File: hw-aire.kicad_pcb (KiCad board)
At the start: 2 copper layers, 75 x 60 mm, 58 parts, among them J1 Conn_01x02_Pin, J2 Conn_01x02_Pin, J3 Screw_Terminal_01x12, J4 Conn_01x04_Pin, J5 Conn_01x05_Pin, K1 JRC-21F(4100), K2 JRC-21F(4100), K3 JRC-21F(4100), Q1 PMBT3904235, Q2 PMBT3904235, Q3 PMBT3904235, Q5 PMBT3904235, SW1 SW_Push, U1 HLK-2M05, U2 NCP1117-3.3_SOT223, U3 ESP-12E, U4 SHT4x, U5 BMP581

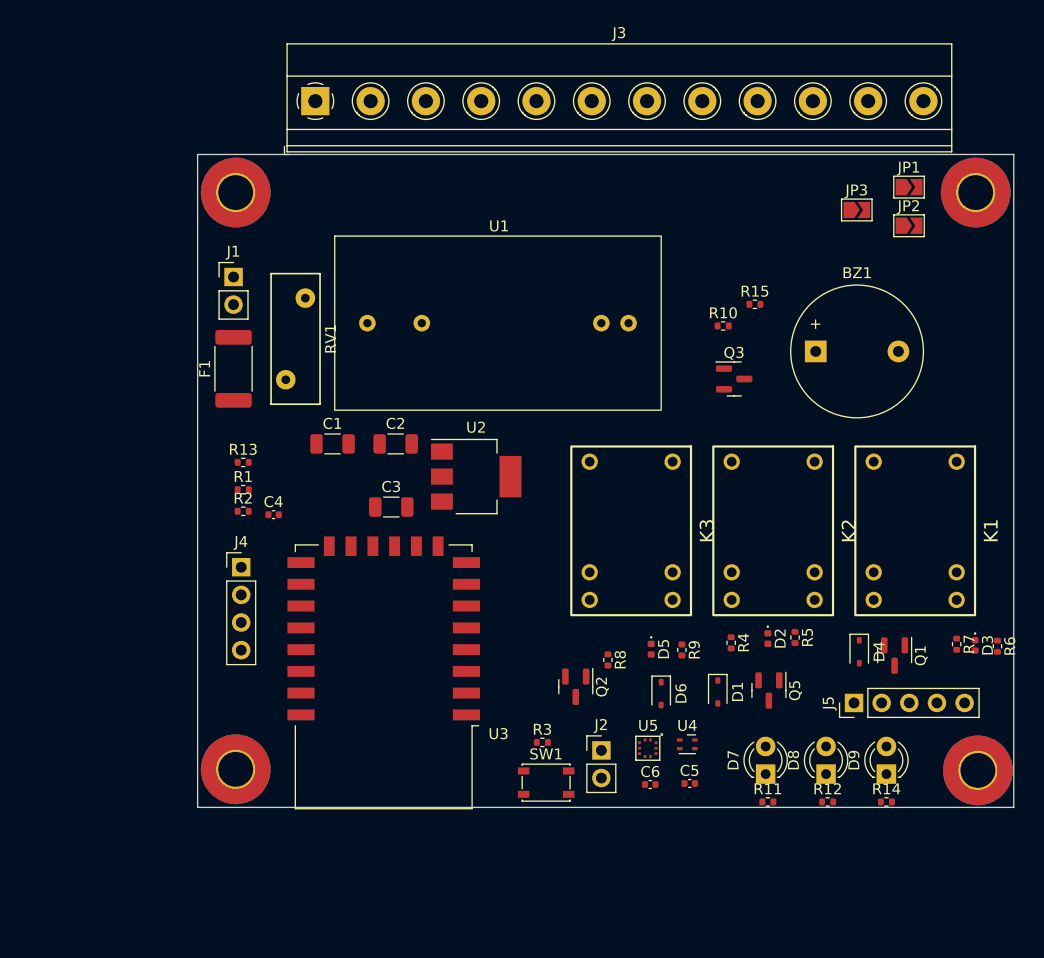
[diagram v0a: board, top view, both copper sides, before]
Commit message: Finish routing and serigraphy. Ready to review
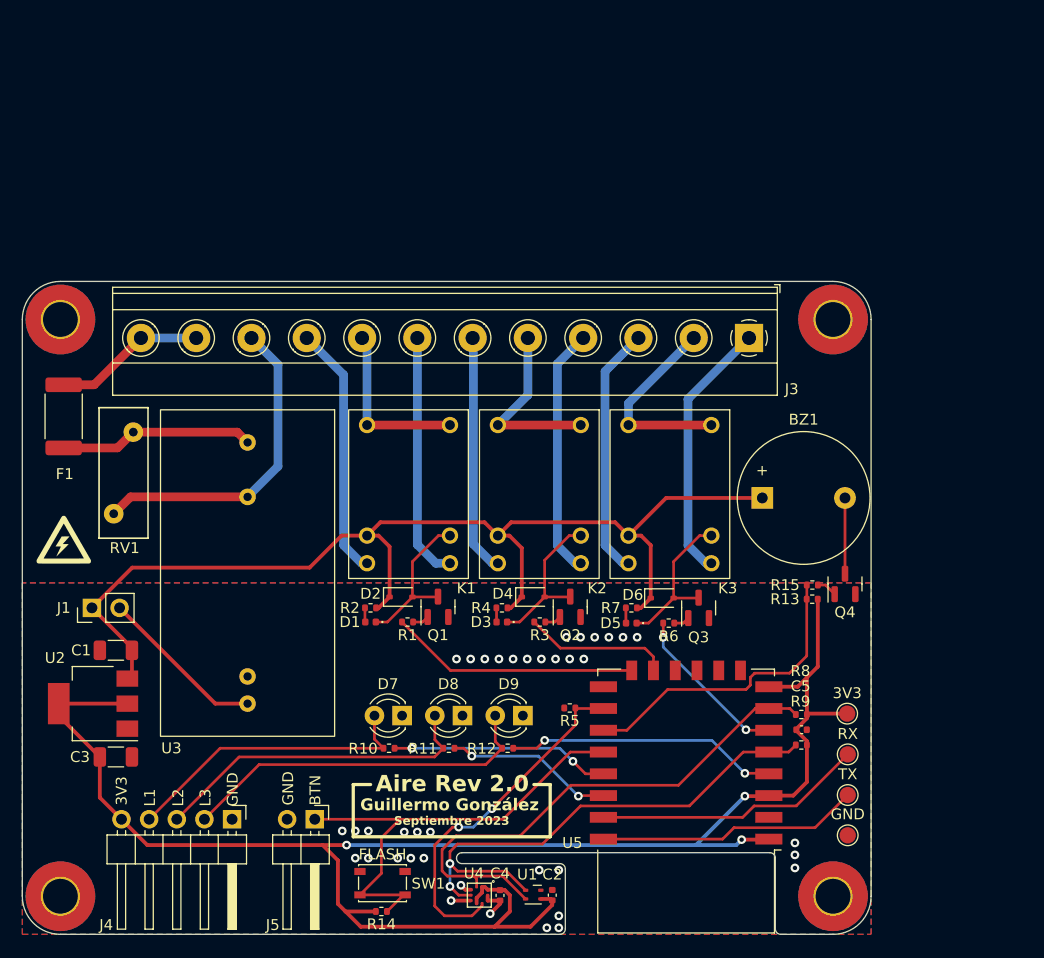
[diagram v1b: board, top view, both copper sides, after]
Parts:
- removed the C3 at (140.7, 87.6)
- removed the J4 at (126.9, 93.1)
- removed JP1, JP2, JP3: SolderJumper_2_Open, Jumper:SolderJumper-2_P1.3mm_Open_TrianglePad1.0x1.5mm
- added G***: LOGO, guille-lib:high_voltage_5mm, F.Cu at (110.6, 90.6)
- added G***: LOGO, guille-lib:high_voltage, B.Cu at (121.6, 88.2)
- added TP1: TestPoint, TestPoint:TestPoint_Pad_D1.5mm, F.Cu at (182.6, 114.1)
- added TP2: TestPoint, TestPoint:TestPoint_Pad_D1.5mm, F.Cu at (182.6, 110.3)
- added TP3: TestPoint, TestPoint:TestPoint_Pad_D1.5mm, F.Cu at (182.6, 117.8)
- added TP4: TestPoint, TestPoint:TestPoint_Pad_D1.5mm, F.Cu at (182.6, 106.6)
- J4: renamed from J5; footprint Connector_PinHeader_2.54mm:PinHeader_1x05_P2.54mm_Vertical -> Connector_PinHeader_2.54mm:PinHeader_1x05_P2.54mm_Horizontal
- J5: renamed from J2; footprint Connector_PinHeader_2.54mm:PinHeader_1x02_P2.54mm_Vertical -> Connector_PinHeader_2.54mm:PinHeader_1x02_P2.54mm_Horizontal
- moved J4 58.1 mm to (126.1, 116.3), turned to -90 degrees
- moved R9 56.4 mm to (178.4, 109.5), turned to 180 degrees
- moved R8 54.6 mm to (178.4, 106.7), turned to 180 degrees
- moved C5 52.4 mm to (178.4, 108.1)
- moved J3 45.4 mm to (173.6, 72.1), turned to 180 degrees
- moved D3 43.5 mm to (150.9, 98.2), turned to 180 degrees
- moved R3 42.1 mm to (154.3, 98.2), turned to 0 degrees
- moved R4 41.9 mm to (150.9, 96.9), turned to 180 degrees
- moved U2 40.9 mm to (113.3, 105.7), turned to 180 degrees
- moved R2 39.1 mm to (138.8, 96.9), turned to 180 degrees
- moved C3 38.6 mm to (115.4, 110.6)
- moved R5 37.5 mm to (157.1, 106.1), turned to 180 degrees
- moved D1 36.5 mm to (138.8, 98.2), turned to 180 degrees
- moved R10 35.2 mm to (140.5, 109.8), turned to 180 degrees
- moved R11 35.2 mm to (146.0, 109.8), turned to 180 degrees
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- renumbered C5 to C2, C2 to C3, C6 to C4, C4 to C5, D2 to D1, D1 to D2, K2 to K1, K1 to K2, Q5 to Q1, Q1 to Q2, Q2 to Q3, Q3 to Q4, R4 to R1, R11 to R10, R12 to R11, R14 to R12, R15 to R13, R3 to R14, R10 to R15, R5 to R2, R6 to R3, R7 to R4, R13 to R5, R8 to R6, R9 to R7, R2 to R8, R1 to R9, U4 to U1, U1 to U3, U5 to U4, U3 to U5
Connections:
- D7 pad 2: Net-(D7-A) -> /LED1R
- D8 pad 2: Net-(D8-A) -> /LED2R
- D9 pad 2: Net-(D9-A) -> /LED3R
- H1 pad 1: GND -> unconnected-(H1-Pad1)
- H2 pad 1: GND -> unconnected-(H2-Pad1)
- J3 pad 1: /NC1 -> /NO3
- J3 pad 10: /L -> /N
- J3 pad 12: /N -> /L
- J3 pad 2: /COM1 -> /COM3
- J3 pad 3: /NO1 -> /NC3
- J3 pad 4: /NC2 -> /NO2
- J3 pad 6: /NO2 -> /NC2
- J3 pad 7: /NC3 -> /NO1
- J3 pad 8: /COM3 -> /COM1
- J3 pad 9: /NO3 -> /NC1
- J4 pad 1: +3V3 -> GND
- J4 pad 2: /LED1 -> /LED3R
- J4 pad 3: /LED2 -> /LED2R
- J4 pad 4: /LED3 -> /LED1R
- J4 pad 5: GND -> +3V3
- R10 pad 2: Net-(D7-A) -> /LED1R
- R11 pad 2: Net-(D8-A) -> /LED2R
- R12 pad 2: Net-(D9-A) -> /LED3R
- U5 pad 13: /LED2 -> /FAN2
- U5 pad 14: /LED1 -> /FAN1
- U5 pad 19: /FAN1 -> /LED1
- U5 pad 20: /FAN2 -> /LED2
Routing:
- net +3V3: track 0.00 -> 158.7 mm, vias 0 -> 3
- net +5V: track 0.00 -> 102.6 mm
- net /I2C_SCL: track 0.00 -> 49.9 mm
- net /I2C_SDA: track 0.00 -> 49.3 mm, vias 0 -> 2
- net /GPIO0: track 0.00 -> 44.3 mm
- net /LED3R: track 0.00 -> 33.3 mm
- net /BMP_INT: track 0.00 -> 32.6 mm, vias 0 -> 2
- net /LED2R: track 0.00 -> 30.5 mm
- net /N: track 0.00 -> 29.7 mm
- net /BUZZ: track 0.00 -> 28.4 mm
- net /LED1R: track 0.00 -> 27.6 mm
- net /TX: track 0.00 -> 25.1 mm
- net /LED3: track 0.00 -> 25.1 mm, vias 0 -> 2
- net /RX: track 0.00 -> 24.8 mm
- net /NO3: track 0.00 -> 24.2 mm
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- added copper zone on B.Cu, net GND
- added copper zone on F.Cu, net GND
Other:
- board size 75 x 60 mm -> 78 x 60 mm
- board text added: "3V3"
- board text added: "Aire Rev 2.0"
- board text added: "BTN"
- board text added: "FLASH"
- board text added: "GND"
- board text added: "Guillermo González"
- board text added: "L1"
- board text added: "L2"
- board text added: "L3"
- board text added: "RX"
- board text added: "Septiembre 2023"
- board text added: "TX"

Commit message: New revision, add IO expander and fix I2C GPIOs
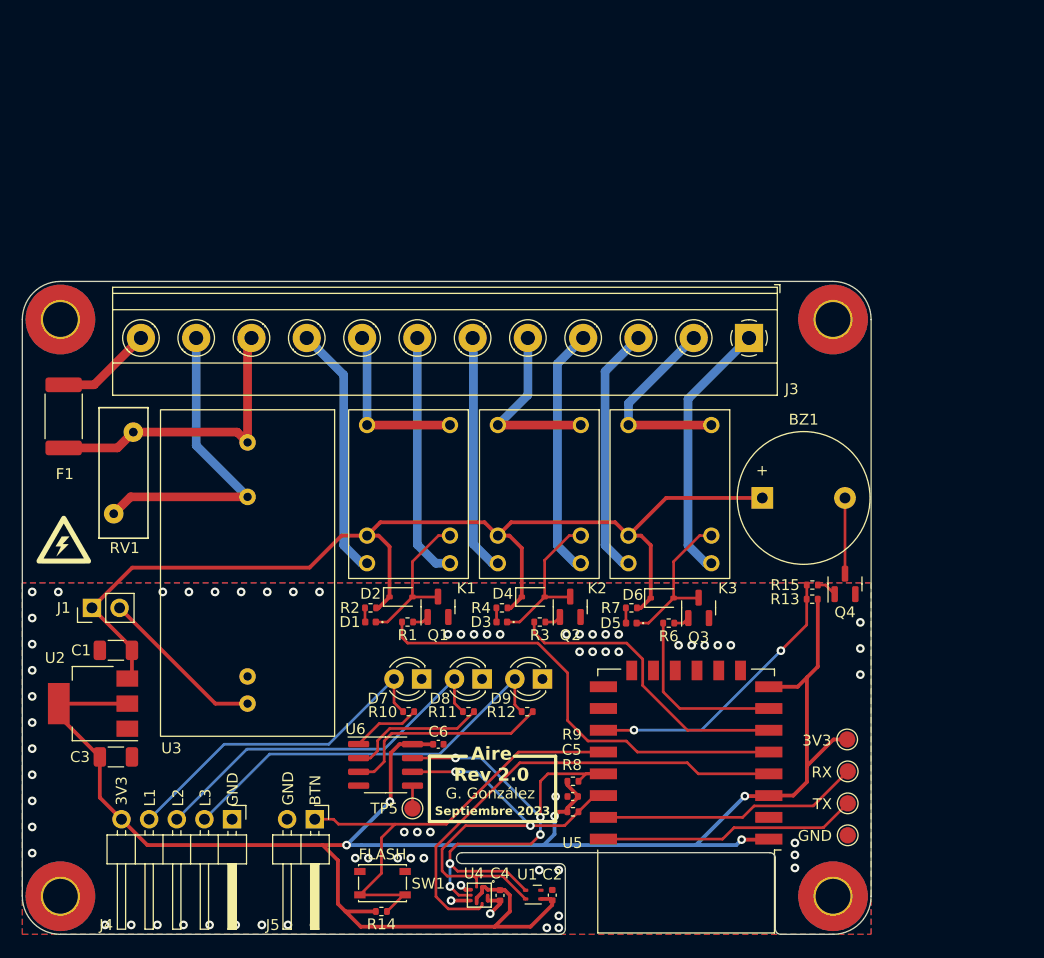
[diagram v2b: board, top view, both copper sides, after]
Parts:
- removed R5: 10k, Resistor_SMD:R_0402_1005Metric
- added C6: 100n, Capacitor_SMD:C_0402_1005Metric, F.Cu at (145.0, 109.4)
- added TP5: TestPoint, TestPoint:TestPoint_Pad_D1.5mm, F.Cu at (142.6, 115.3)
- added U6: PCA9536D, Package_SO:SOIC-8_3.9x4.9mm_P1.27mm, F.Cu at (140.2, 111.3)
- moved R8 22.8 mm to (157.4, 115.6), turned to 0 degrees
- moved C5 21.9 mm to (157.4, 114.2), turned to 180 degrees
- moved R9 21.3 mm to (157.4, 112.8), turned to 0 degrees
- moved D7 3.82 mm to (143.5, 103.4)
- moved D9 3.82 mm to (154.6, 103.4)
- moved R12 3.82 mm to (153.2, 106.4)
- moved D8 3.82 mm to (149.0, 103.4)
- moved R10 3.82 mm to (142.3, 106.4)
- moved R11 3.82 mm to (147.8, 106.4)
- moved TP4 2.37 mm to (182.6, 109.0)
- moved TP2 1.56 mm to (182.6, 111.9)
- moved TP1 0.76 mm to (182.6, 114.8)
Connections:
- H3 pad 1: GND -> unconnected-(H3-Pad1)
- H4 pad 1: GND -> unconnected-(H4-Pad1)
- J3 pad 10: /N -> /LF
- J3 pad 11: /L -> /N
- U5 pad 13: /FAN2 -> unconnected-(U5-MOSI-Pad13)
- U5 pad 14: /FAN1 -> unconnected-(U5-SCLK-Pad14)
- U5 pad 16: /BMP_INT -> GND
- U5 pad 19: /LED1 -> /I2C_SDA
- U5 pad 20: /LED2 -> /I2C_SCL
- U5 pad 4: /LED3 -> /BMP_INT
- U5 pad 5: /I2C_SDA -> /FAN1
- U5 pad 6: /FAN3 -> /FAN2
- U5 pad 7: /I2C_SCL -> /FAN3
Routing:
- net +3V3: track 158.7 -> 181.3 mm, vias 3 -> 5
- net /FAN1: track 23.0 -> 42.1 mm
- net /FAN2: track 13.5 -> 27.7 mm
- net /LED1: track 20.2 -> 6.34 mm, vias 2 -> 0
- net /BMP_INT: track 32.6 -> 43.9 mm, vias 2 -> 0
- net /LF: track 17.9 -> 27.6 mm
- net /I2C_SCL: track 49.9 -> 41.6 mm, vias 0 -> 2
- net /LED3: track 25.1 -> 19.4 mm, vias 2 -> 0
- net /L: track 14.0 -> 8.88 mm
- net /LED3R: track 33.3 -> 37.1 mm
- net /LED2R: track 30.5 -> 34.2 mm
- net /LED1R: track 27.6 -> 31.2 mm
- net /LED2: track 15.5 -> 12.9 mm, vias 2 -> 0
- net Net-(U6-IO3): track 0.00 -> 2.10 mm
- net /BUZZ: track 28.4 -> 26.4 mm, vias 0 -> 2
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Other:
- board text added: "G. González"
